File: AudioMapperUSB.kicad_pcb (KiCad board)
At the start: 2 copper layers, 100 x 100 mm, 160 parts, among them J1 USB_B, J10 Conn_01x01, J11 Conn_01x01, J12 Jack-DC, J13 Conn_01x02, J14 Conn_01x02, J16 Audio-Jack-2, J17 Audio-Jack-2, J18 Audio-Jack-2, J19 Audio-Jack-2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

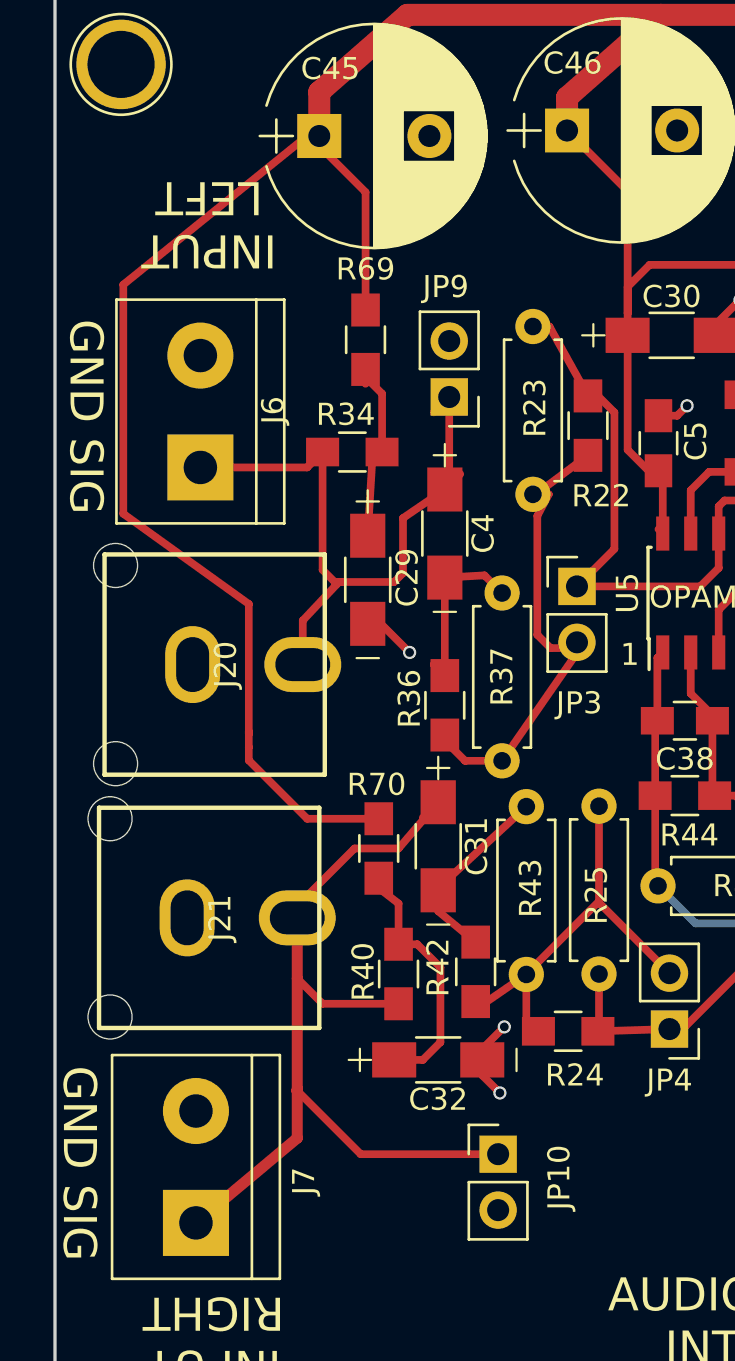
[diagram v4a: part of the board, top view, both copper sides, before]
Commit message: Added source code of Audiomapper
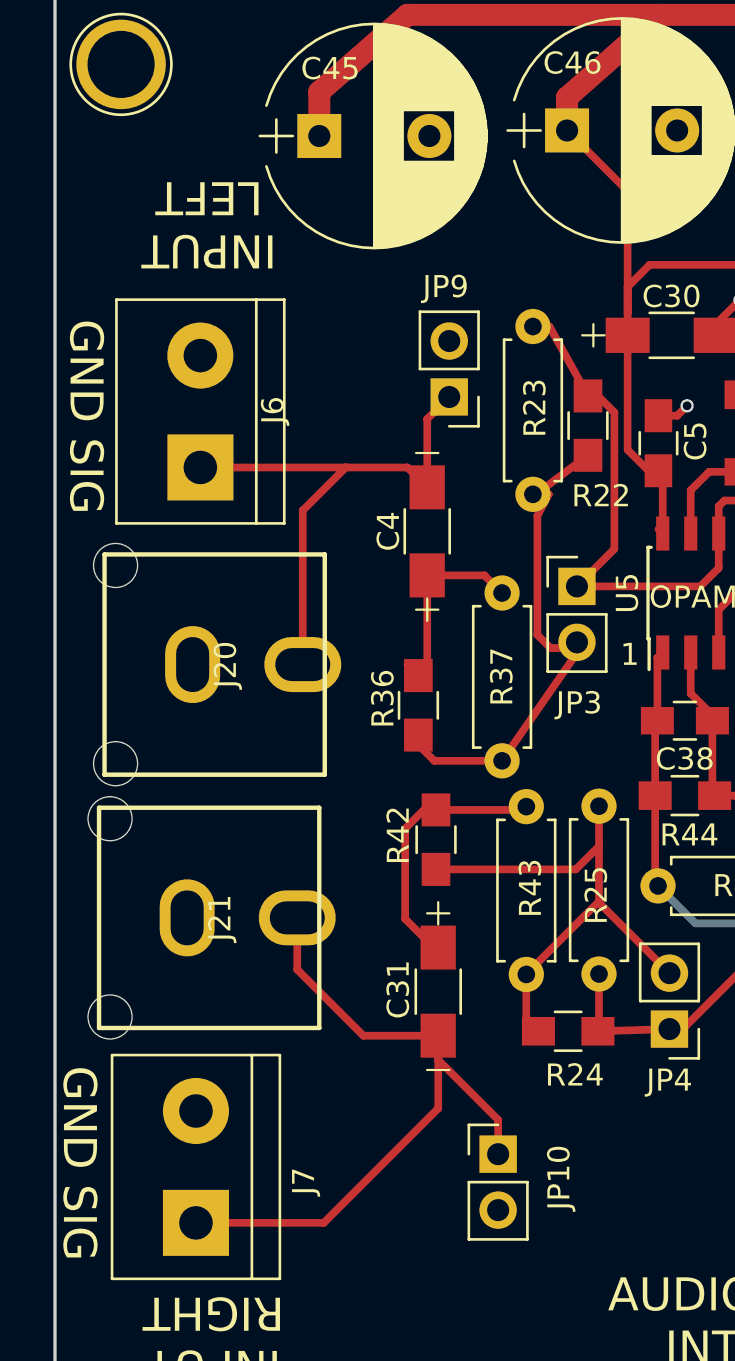
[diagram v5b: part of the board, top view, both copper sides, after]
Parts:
- removed C29, C32: 10 uF, AudioMapperUSB:CP_1206_HandSoldering
- removed R34, R40: 4k7, Resistors_SMD:R_0805_HandSoldering
- removed R69, R70: 1k, Resistors_SMD:R_0805_HandSoldering
- moved C31 6.60 mm to (47.4, 75.1)
- moved R42 6.26 mm to (47.3, 68.2)
- moved R36 1.20 mm to (46.5, 62.1)
- moved C4 0.81 mm to (46.9, 54.2), turned to 90 degrees
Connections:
- J20 pad 1: Net-(C4-Pad1) -> Net-(C4-Pad2)
- J21 pad 1: Net-(C31-Pad1) -> Net-(C31-Pad2)
- J6 pad 1: Net-(C4-Pad1) -> Net-(C4-Pad2)
- J7 pad 1: Net-(C31-Pad1) -> Net-(C31-Pad2)
- JP10 pad 1: Net-(C31-Pad1) -> Net-(C31-Pad2)
- JP9 pad 1: Net-(C4-Pad1) -> Net-(C4-Pad2)
- R36 pad 2: Net-(C4-Pad2) -> Net-(C4-Pad1)
- R37 pad 1: Net-(C4-Pad2) -> Net-(C4-Pad1)
- R42 pad 2: Net-(C31-Pad2) -> Net-(C31-Pad1)
- R43 pad 1: Net-(C31-Pad2) -> Net-(C31-Pad1)
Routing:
- net Net-(C1-Pad1): track 452.9 -> 402.2 mm
- net Net-(C31-Pad1): track 44.1 -> 12.1 mm
- net Net-(C31-Pad2): track 10.3 -> 34.5 mm
- net Net-(C4-Pad1): track 32.8 -> 9.15 mm
- net Net-(C4-Pad2): track 9.22 -> 25.4 mm
- net Net-(C32-Pad1): track 12.1 -> 0.00 mm
- net Net-(C29-Pad1): track 8.70 -> 0.00 mm
- net GND: track 144.6 -> 137.6 mm, vias 66 -> 63
- net Net-(JP4-Pad2): track 19.5 -> 24.6 mm
- net Net-(JP3-Pad2): track 22.1 -> 23.7 mm

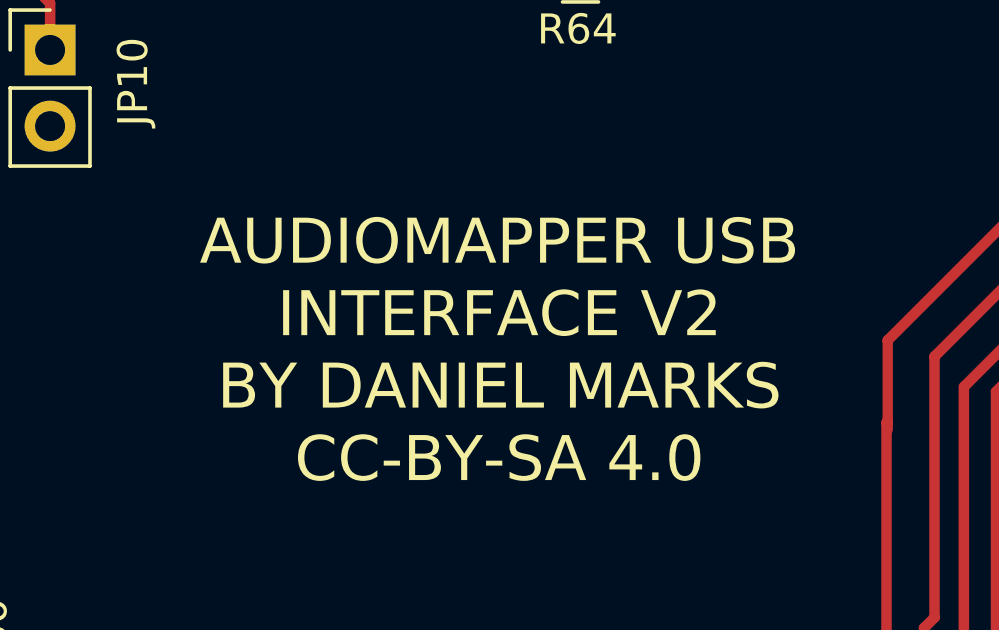
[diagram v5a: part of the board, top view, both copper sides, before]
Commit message: Fixed JLCPCB BOM/placement
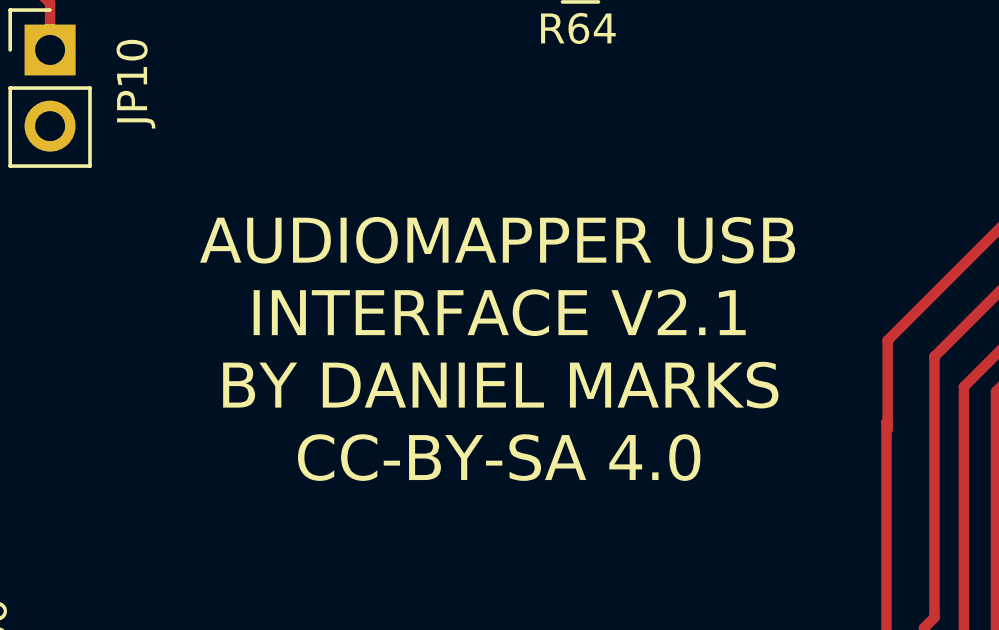
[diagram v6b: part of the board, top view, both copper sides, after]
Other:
- board text added: "AUDIOMAPPER USB INTERFACE V2.1 BY DANIEL MARKS CC-BY-SA 4.0"
- board text removed: "AUDIOMAPPER USB INTERFACE V2 BY DANIEL MARKS CC-BY-SA 4.0"
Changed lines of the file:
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@@
   )
   (setup
-    (last_trace_width 0.35)
+    (last_trace_width 0.25)
     (user_trace_width 0.35)
     (user_trace_width 0.5)
@@
     (effects (font (size 1 1) (thickness 0.15)))
   )
-  (gr_text "AUDIOMAPPER USB\nINTERFACE V2\nBY DANIEL MARKS\nCC-BY-SA 4.0" (at 65.1 92.5) (layer F.SilkS)
+  (gr_text "AUDIOMAPPER USB\nINTERFACE V2.1\nBY DANIEL MARKS\nCC-BY-SA 4.0" (at 65.1 92.5) (layer F.SilkS)
     (effects (font (size 1.5 1.5) (thickness 0.3)))
   )

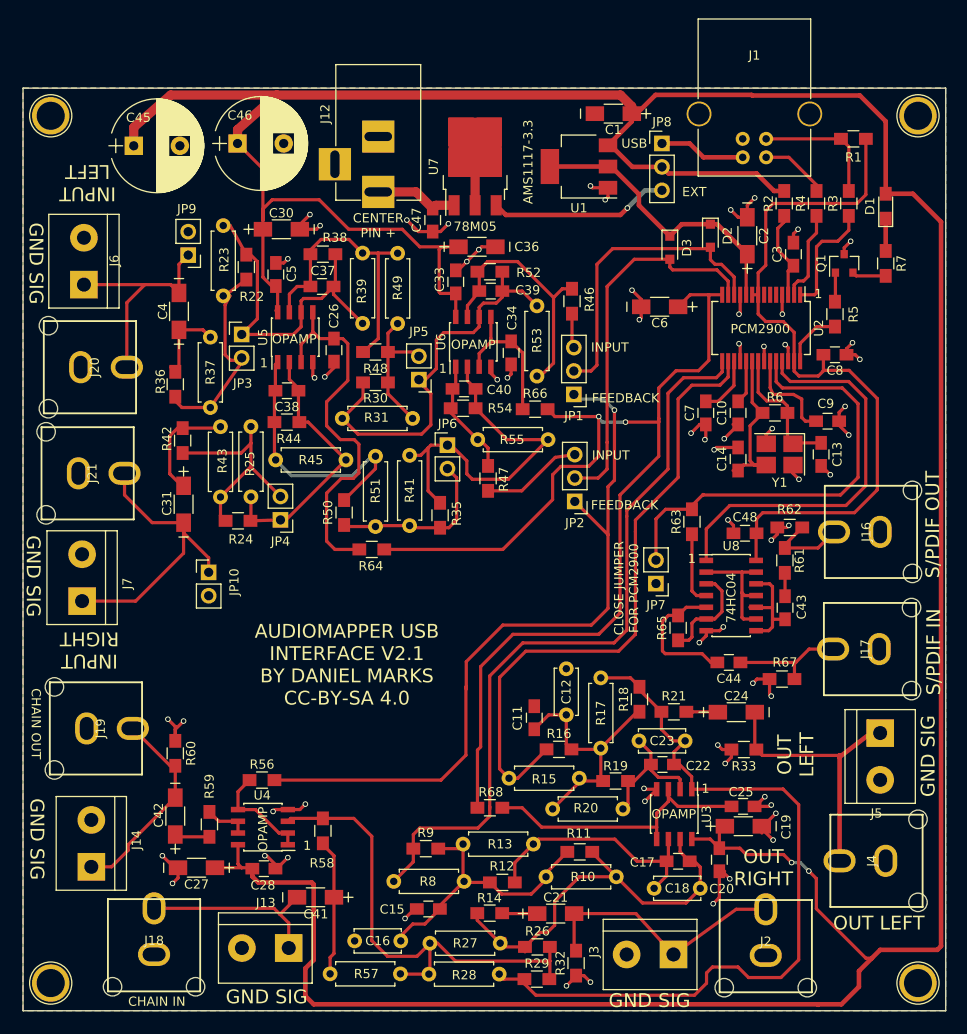
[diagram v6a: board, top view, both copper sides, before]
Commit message: Added balanced outputs
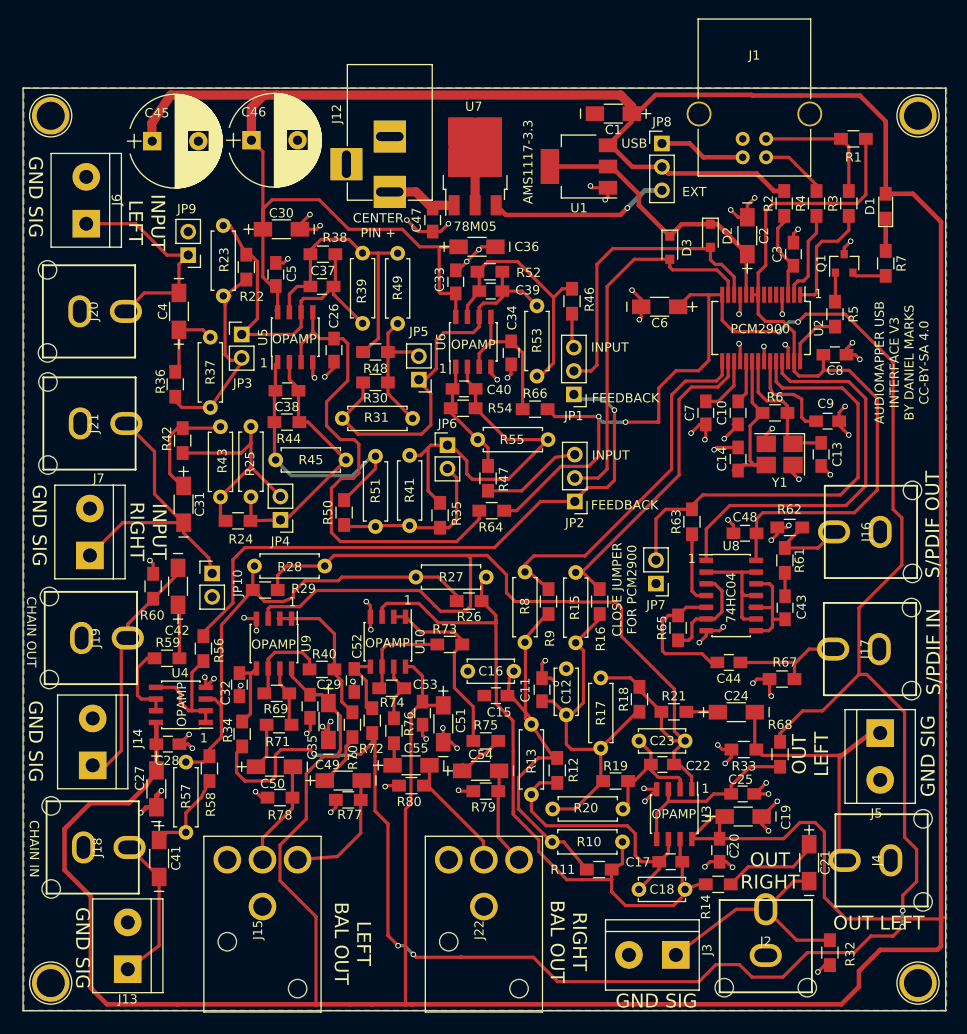
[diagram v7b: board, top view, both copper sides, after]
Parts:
- added C29: 10 uF, AudioMapperUSB:CP_1206_HandSoldering, F.Cu at (63.1, 98.7)
- added C32: 1 uF, Capacitors_SMD:C_0805_HandSoldering, F.Cu at (53.5, 94.7)
- added C35: 1 uF, Capacitors_SMD:C_0805_HandSoldering, F.Cu at (61.1, 97.0)
- added C49: 10 uF, AudioMapperUSB:CP_1206_HandSoldering, F.Cu at (64.7, 105.0)
- added C50: 10 uF, AudioMapperUSB:CP_1206_HandSoldering, F.Cu at (57.2, 103.5)
- added C51: 10 uF, AudioMapperUSB:CP_1206_HandSoldering, F.Cu at (75.5, 98.9)
- added C52: 1 uF, Capacitors_SMD:C_0805_HandSoldering, F.Cu at (65.9, 94.2)
- added C53: 1 uF, Capacitors_SMD:C_0805_HandSoldering, F.Cu at (73.3, 97.8)
- added C54: 10 uF, AudioMapperUSB:CP_1206_HandSoldering, F.Cu at (79.6, 104.0)
- added C55: 10 uF, AudioMapperUSB:CP_1206_HandSoldering, F.Cu at (72.0, 103.4)
- added J15: XLR4BODYPIN, AudioMapperUSB:IOXLR3MEH, F.Cu at (56.0, 121.2)
- added J22: XLR4BODYPIN, AudioMapperUSB:IOXLR3MEH, F.Cu at (80.0, 121.2)
- added R34: 100R, Resistors_SMD:R_0805_HandSoldering, F.Cu at (53.8, 100.0)
- added R40: 10k, Resistors_SMD:R_0805_HandSoldering, F.Cu at (62.4, 93.0)
- added R69: 10k, Resistors_SMD:R_0805_HandSoldering, F.Cu at (57.5, 95.6)
- added R70: 100R, Resistors_SMD:R_0805_HandSoldering, F.Cu at (65.7, 99.0)
- added R71: 100R, Resistors_SMD:R_0805_HandSoldering, F.Cu at (57.8, 99.0)
- added R72: 100R, Resistors_SMD:R_0805_HandSoldering, F.Cu at (67.8, 98.5)
- added R73: 10k, Resistors_SMD:R_0805_HandSoldering, F.Cu at (76.2, 90.3)
- added R74: 10k, Resistors_SMD:R_0805_HandSoldering, F.Cu at (70.0, 95.0)
- added R75: 100R, Resistors_SMD:R_0805_HandSoldering, F.Cu at (80.2, 100.8)
- added R76: 100R, Resistors_SMD:R_0805_HandSoldering, F.Cu at (70.2, 99.7)
- added R77: 1M, Resistors_SMD:R_0805_HandSoldering, F.Cu at (65.2, 107.2)
- added R78: 1M, Resistors_SMD:R_0805_HandSoldering, F.Cu at (57.9, 106.9)
- added R79: 1M, Resistors_SMD:R_0805_HandSoldering, F.Cu at (80.2, 106.2)
- added R80: 1M, Resistors_SMD:R_0805_HandSoldering, F.Cu at (72.1, 105.6)
- added U10: OPA2170, Housings_SOIC:SOIC-8_3.9x4.9mm_Pitch1.27mm, F.Cu at (69.5, 90.0)
- added U9: OPA2170, Housings_SOIC:SOIC-8_3.9x4.9mm_Pitch1.27mm, F.Cu at (57.2, 90.2)
- moved R29 51.4 mm to (56.2, 84.4), turned to 180 degrees
- moved R28 48.1 mm to (62.7, 81.8)
- moved R27 39.7 mm to (80.2, 83.0)
- moved R26 38.2 mm to (78.3, 85.6), turned to 180 degrees
- moved R8 36.4 mm to (84.4, 82.5), turned to 270 degrees
- moved R57 32.7 mm to (47.6, 103.0), turned to 270 degrees
- moved R68 32.0 mm to (112.0, 102.2), turned to 90 degrees
- moved C16 31.7 mm to (78.2, 93.2)
- moved R9 29.9 mm to (87.0, 85.7), turned to 270 degrees
- moved C21 28.0 mm to (115.2, 114.0), turned to 270 degrees
- moved R32 27.5 mm to (117.5, 123.7)
- moved R14 25.0 mm to (105.3, 116.3)
- moved C42 24.9 mm to (46.8, 84.0)
- moved C15 24.3 mm to (81.2, 95.8)
- moved R15 23.4 mm to (89.9, 82.5), turned to 270 degrees
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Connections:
- net Net-(C1-Pad1) renamed VBUS
- net Net-(C17-Pad2) renamed RIGHTCH
- net Net-(C22-Pad2) renamed LEFTCH
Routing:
- net VCOM: track 125.1 -> 264.3 mm, vias 2 -> 10
- net VBUS: track 402.2 -> 533.1 mm, vias 2 -> 0
- net VOUTR: track 83.0 -> 40.2 mm
- net RIGHTCH: track 44.5 -> 81.6 mm
- net VOUTL: track 68.9 -> 35.1 mm
- net LEFTCH: track 86.3 -> 111.5 mm
- net Net-(R73-Pad2): track 0.00 -> 20.6 mm
- net GND: track 137.6 -> 155.5 mm, vias 63 -> 78
- net Net-(R40-Pad2): track 0.00 -> 16.4 mm
- net Net-(C49-Pad2): track 0.00 -> 15.2 mm
- net Net-(JP1-Pad1): track 82.0 -> 67.7 mm
- net Net-(C55-Pad2): track 0.00 -> 14.2 mm
- net Net-(C26-Pad1): track 41.1 -> 54.4 mm
- net Net-(C15-Pad2): track 31.1 -> 44.0 mm
- net Net-(C54-Pad2): track 0.00 -> 12.8 mm
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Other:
- board text added: "AUDIOMAPPER USB INTERFACE V3 BY DANIEL MARKS CC-BY-SA 4.0"
- board text added: "LEFT BAL OUT"
- board text added: "RIGHT BAL OUT"
- board text removed: "AUDIOMAPPER USB INTERFACE V2.1 BY DANIEL MARKS CC-BY-SA 4.0"
